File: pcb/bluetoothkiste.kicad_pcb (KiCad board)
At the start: 2 copper layers, 44.9 x 95.6 mm, 58 parts, among them J1 DB9_Female, J2 Screw_Terminal_01x03, J3 Conn_01x04_Female, J4 RJ45, J6 Conn_01x04_Female, U1 L7805, U2 MAX232

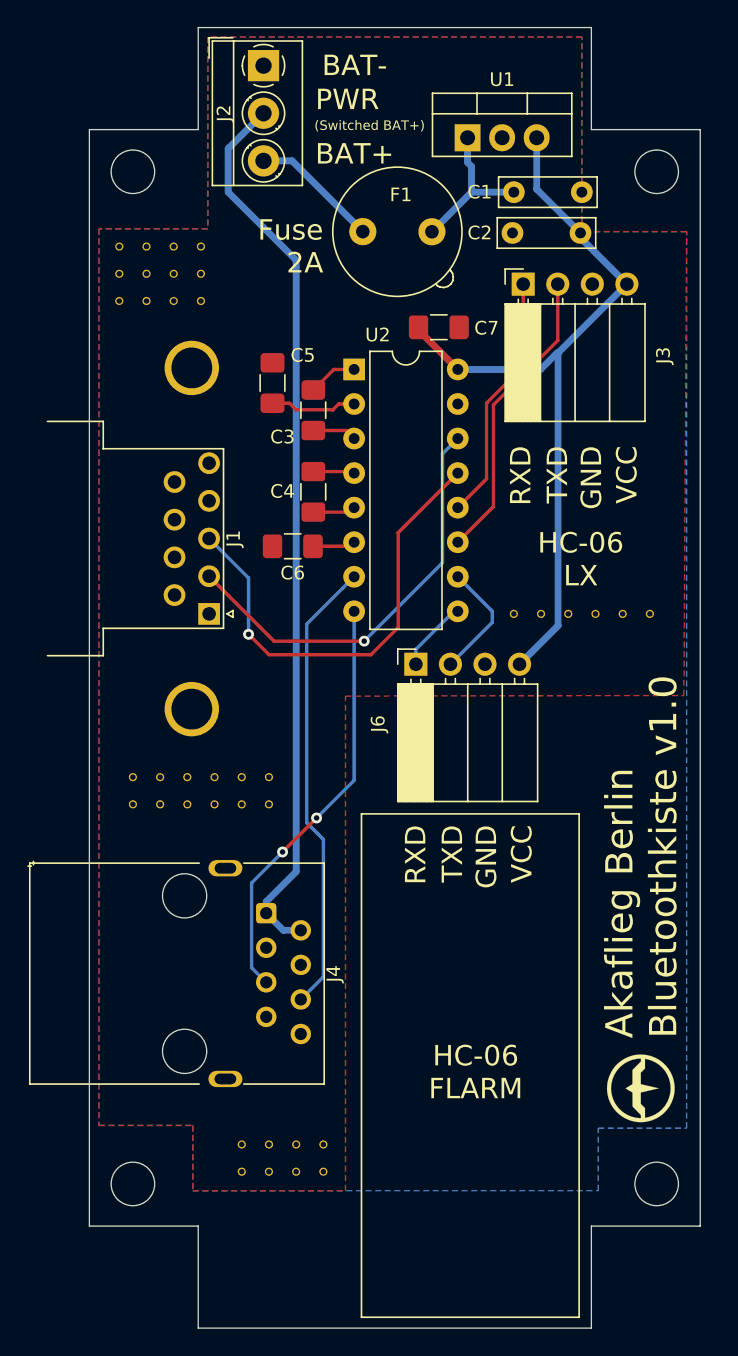
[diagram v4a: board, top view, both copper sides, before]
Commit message: layout updated
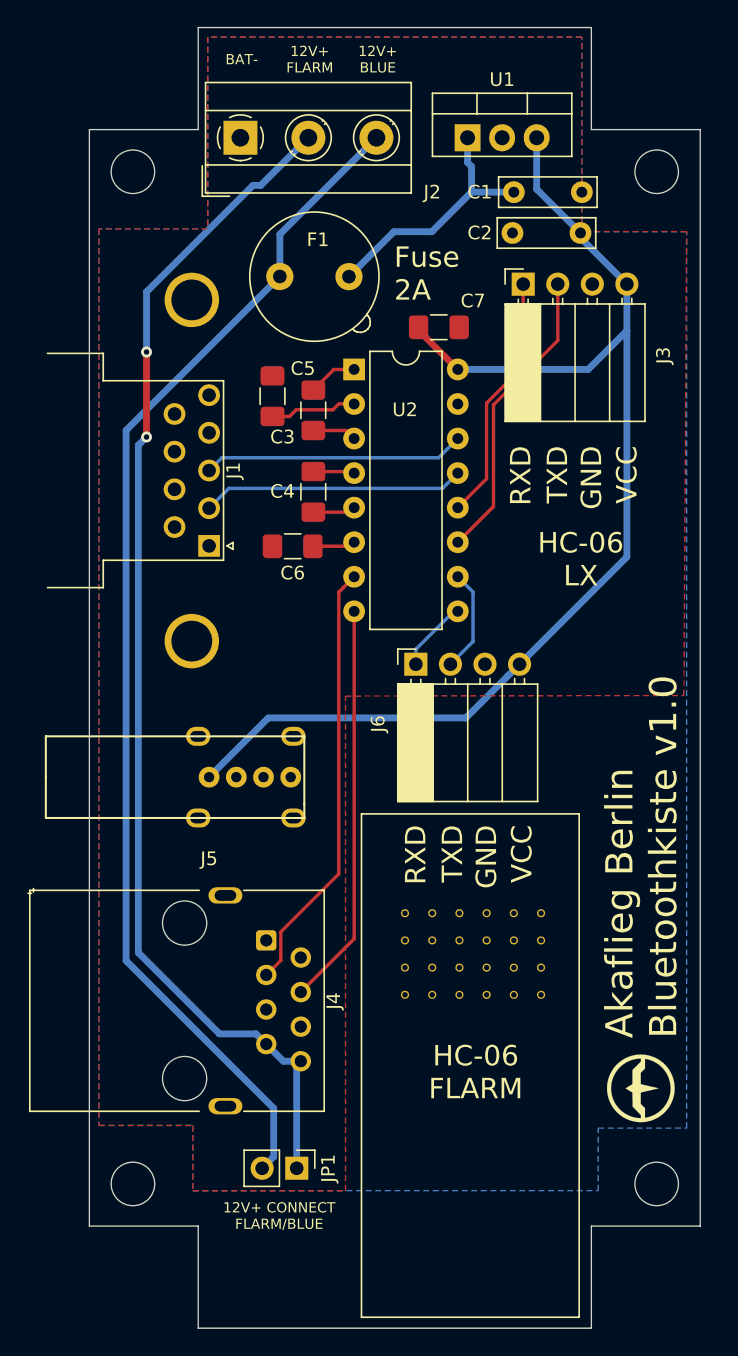
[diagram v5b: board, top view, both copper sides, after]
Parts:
- removed the REF** at (187.0, 60.0)
- removed the REF** at (169.0, 74.0)
- removed the REF** at (164.0, 33.0)
- removed the REF** at (158.0, 37.0)
- removed the REF** at (158.0, 35.0)
- removed the REF** at (164.0, 35.0)
- removed the REF** at (162.0, 37.0)
- removed the REF** at (160.0, 35.0)
- removed the REF** at (160.0, 37.0)
- removed the REF** at (162.0, 35.0)
- removed the REF** at (164.0, 37.0)
- removed the REF** at (191.0, 60.0)
- removed the REF** at (161.0, 74.0)
- removed the REF** at (161.0, 72.0)
- removed the REF** at (163.0, 72.0)
- removed the REF** at (165.0, 72.0)
- removed the REF** at (165.0, 74.0)
- removed the REF** at (163.0, 74.0)
- removed the REF** at (159.0, 72.0)
- removed the REF** at (159.0, 74.0)
- removed the REF** at (167.0, 101.0)
- removed the REF** at (195.0, 60.0)
- removed the REF** at (169.0, 101.0)
- removed the REF** at (171.0, 101.0)
- removed the REF** at (173.0, 101.0)
- removed the REF** at (173.0, 99.0)
- removed the REF** at (171.0, 99.0)
- removed the REF** at (169.0, 99.0)
- removed the REF** at (167.0, 99.0)
- removed the REF** at (162.0, 33.0)
- removed the REF** at (160.0, 33.0)
- removed the REF** at (158.0, 33.0)
- removed the REF** at (197.0, 60.0)
- removed the REF** at (189.0, 60.0)
- removed the REF** at (193.0, 60.0)
- removed the REF** at (169.0, 72.0)
- removed the REF** at (167.0, 74.0)
- removed the REF** at (167.0, 72.0)
- added J5: USB_A, JS_Local:USB_A_UPRIGHT_SEGOR, F.Cu at (164.6, 72.0)
- added JP1: Jumper, Connector_PinHeader_2.54mm:PinHeader_1x02_P2.54mm_Vertical, F.Cu at (171.0, 100.8)
- added REF**: VIA-0.6mm, JS_Local:VIA-0.6mm, F.Cu at (187.0, 82.0)
- added REF**: VIA-0.6mm, JS_Local:VIA-0.6mm, F.Cu at (179.0, 84.0)
- added REF**: VIA-0.6mm, JS_Local:VIA-0.6mm, F.Cu at (181.0, 84.0)
- added REF**: VIA-0.6mm, JS_Local:VIA-0.6mm, F.Cu at (183.0, 82.0)
- added REF**: VIA-0.6mm, JS_Local:VIA-0.6mm, F.Cu at (187.0, 88.0)
- added REF**: VIA-0.6mm, JS_Local:VIA-0.6mm, F.Cu at (189.0, 86.0)
- added REF**: VIA-0.6mm, JS_Local:VIA-0.6mm, F.Cu at (185.0, 86.0)
- added REF**: VIA-0.6mm, JS_Local:VIA-0.6mm, F.Cu at (187.0, 86.0)
- added REF**: VIA-0.6mm, JS_Local:VIA-0.6mm, F.Cu at (185.0, 88.0)
- added REF**: VIA-0.6mm, JS_Local:VIA-0.6mm, F.Cu at (189.0, 88.0)
- added REF**: VIA-0.6mm, JS_Local:VIA-0.6mm, F.Cu at (183.0, 88.0)
- added REF**: VIA-0.6mm, JS_Local:VIA-0.6mm, F.Cu at (185.0, 82.0)
- added REF**: VIA-0.6mm, JS_Local:VIA-0.6mm, F.Cu at (179.0, 88.0)
- added REF**: VIA-0.6mm, JS_Local:VIA-0.6mm, F.Cu at (181.0, 88.0)
- added REF**: VIA-0.6mm, JS_Local:VIA-0.6mm, F.Cu at (183.0, 86.0)
- added REF**: VIA-0.6mm, JS_Local:VIA-0.6mm, F.Cu at (181.0, 86.0)
- added REF**: VIA-0.6mm, JS_Local:VIA-0.6mm, F.Cu at (179.0, 86.0)
- added REF**: VIA-0.6mm, JS_Local:VIA-0.6mm, F.Cu at (189.0, 84.0)
- added REF**: VIA-0.6mm, JS_Local:VIA-0.6mm, F.Cu at (185.0, 84.0)
- added REF**: VIA-0.6mm, JS_Local:VIA-0.6mm, F.Cu at (187.0, 84.0)
- added REF**: VIA-0.6mm, JS_Local:VIA-0.6mm, F.Cu at (189.0, 82.0)
- added REF**: VIA-0.6mm, JS_Local:VIA-0.6mm, F.Cu at (179.0, 82.0)
- added REF**: VIA-0.6mm, JS_Local:VIA-0.6mm, F.Cu at (181.0, 82.0)
- added REF**: VIA-0.6mm, JS_Local:VIA-0.6mm, F.Cu at (183.0, 84.0)
- J2: footprint TerminalBlock_MetzConnect:TerminalBlock_MetzConnect_Type059_RT06303HBWC_1x03_P3.50mm_Horizontal -> TerminalBlock_MetzConnect:TerminalBlock_MetzConnect_Type055_RT01503HDWU_1x03_P5.00mm_Horizontal
- moved F1 6.94 mm to (169.8, 35.2)
- moved J2 5.57 mm to (166.9, 25.0), turned to 0 degrees
- moved J1 5.00 mm to (164.6, 55.0)
- moved J4 2.00 mm to (168.8, 84.0)
- moved C5 0.97 mm to (169.3, 44.0)
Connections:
- J1 pad 2: /LX-RX -> /LX-TX
- J1 pad 3: /LX-TX -> /LX-RX
- J4 pad 1: +12V -> GND
- J4 pad 2: +12V -> GND
- J4 pad 3: (no net) -> /FLARM-RX
- J4 pad 4: GND -> /FLARM-TX
- J4 pad 5: /FLARM-TX -> GND
- J4 pad 6: /FLARM-RX -> (no net)
- J4 pad 7: GND -> +12V
- J4 pad 8: GND -> +12V
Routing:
- net +12P: track 9.45 -> 88.2 mm
- net +5V: track 56.9 -> 88.9 mm
- net +12V: track 65.9 -> 88.7 mm, vias 0 -> 2
- net /LX-TX: track 33.9 -> 19.3 mm, vias 1 -> 0
- net /LX-RX: track 31.1 -> 19.3 mm, vias 1 -> 0
- net Net-(C1-Pad1): track 11.3 -> 18.8 mm
- net /FLARM-RX: track 33.7 -> 31.9 mm
- net /FLARM-TX: track 30.8 -> 29.6 mm, vias 2 -> 0
- net /FLARM-BT-TX: track 8.75 -> 7.59 mm
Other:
- net class Broader added: clearance 0.4, trace_width 0.5, via_dia 0.8, via_drill 0.4
- board text added: "12V+ BLUE"
- board text added: "12V+ CONNECT FLARM/BLUE"
- board text added: "12V+ FLARM"
- board text removed: "(Switched BAT+)"
- board text removed: "BAT+"
- board text removed: "PWR"

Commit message: dioden verpolungsschutz
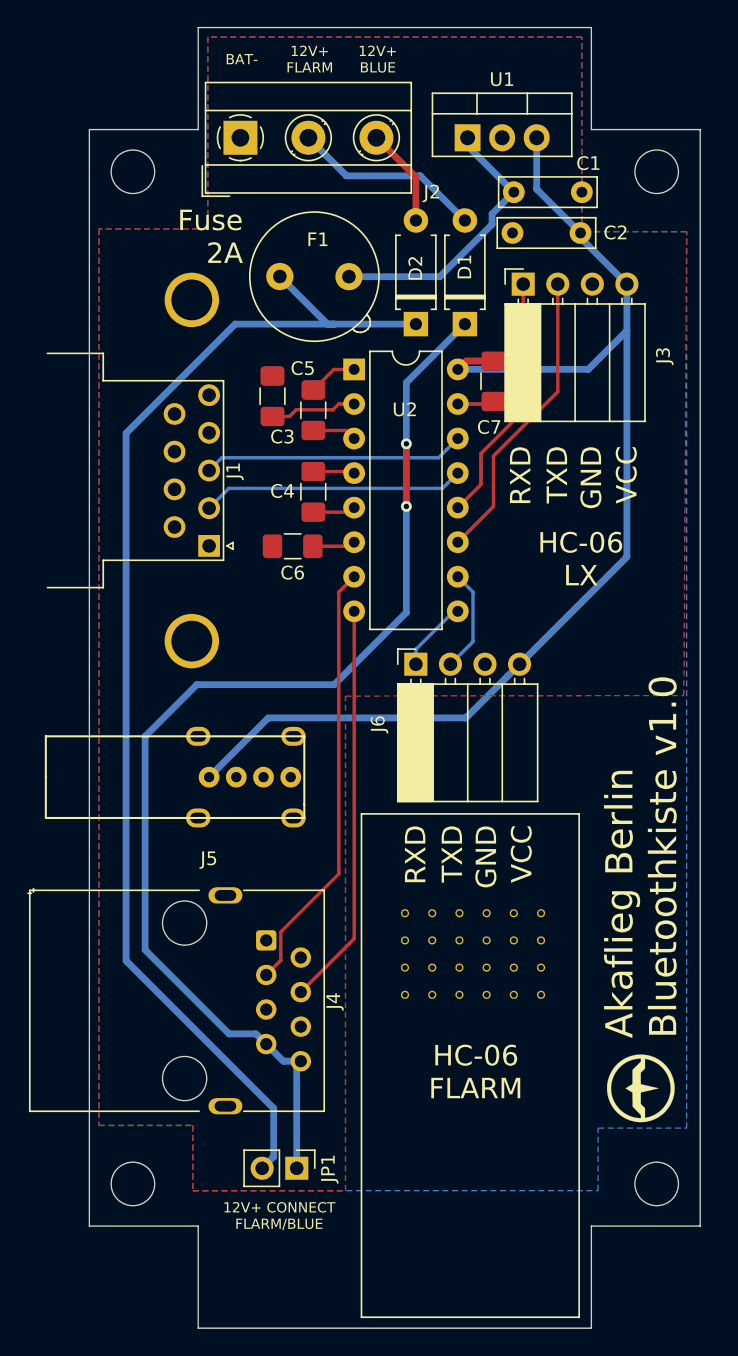
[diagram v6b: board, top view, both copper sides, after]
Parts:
- added D1: D, Diode_THT:D_A-405_P7.62mm_Horizontal, F.Cu at (183.4, 38.7)
- added D2: D, Diode_THT:D_A-405_P7.62mm_Horizontal, F.Cu at (179.8, 38.7)
- moved C7 5.64 mm to (185.5, 42.9), turned to 270 degrees
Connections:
- J2 pad 2: +12V -> Net-(D1-Pad2)
- J2 pad 3: +12P -> Net-(D2-Pad2)
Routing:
- net Net-(D1-Pad2): track 0.00 -> 14.0 mm
- net Net-(D2-Pad2): track 0.00 -> 7.28 mm
- net +12V: track 88.7 -> 84.5 mm
- net GND: track 0.00 -> 2.70 mm
- net Net-(C1-Pad1): track 18.8 -> 20.6 mm
- net +5V: track 88.9 -> 87.5 mm
- net +12P: track 88.2 -> 88.9 mm

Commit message: antennendistanz
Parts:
- removed the REF** at (187.0, 82.0)
- removed the REF** at (183.0, 82.0)
- removed the REF** at (187.0, 88.0)
- removed the REF** at (189.0, 86.0)
- removed the REF** at (185.0, 88.0)
- removed the REF** at (189.0, 88.0)
- removed the REF** at (183.0, 88.0)
- removed the REF** at (185.0, 82.0)
- removed the REF** at (189.0, 84.0)
- removed the REF** at (185.0, 84.0)
- removed the REF** at (187.0, 84.0)
- removed the REF** at (189.0, 82.0)
- removed the REF** at (183.0, 84.0)
- added REF**: VIA-0.6mm, JS_Local:VIA-0.6mm, F.Cu at (157.5, 37.0)
- added REF**: VIA-0.6mm, JS_Local:VIA-0.6mm, F.Cu at (172.0, 79.0)
- added REF**: VIA-0.6mm, JS_Local:VIA-0.6mm, F.Cu at (170.0, 77.0)
- added REF**: VIA-0.6mm, JS_Local:VIA-0.6mm, F.Cu at (168.0, 77.0)
- added REF**: VIA-0.6mm, JS_Local:VIA-0.6mm, F.Cu at (172.0, 59.0)
- added REF**: VIA-0.6mm, JS_Local:VIA-0.6mm, F.Cu at (170.0, 59.0)
- added REF**: VIA-0.6mm, JS_Local:VIA-0.6mm, F.Cu at (170.0, 61.0)
- added REF**: VIA-0.6mm, JS_Local:VIA-0.6mm, F.Cu at (172.0, 61.0)
- added REF**: VIA-0.6mm, JS_Local:VIA-0.6mm, F.Cu at (168.0, 61.0)
- added REF**: VIA-0.6mm, JS_Local:VIA-0.6mm, F.Cu at (157.5, 35.0)
- added REF**: VIA-0.6mm, JS_Local:VIA-0.6mm, F.Cu at (168.0, 59.0)
- added REF**: VIA-0.6mm, JS_Local:VIA-0.6mm, F.Cu at (159.5, 37.0)
- added REF**: VIA-0.6mm, JS_Local:VIA-0.6mm, F.Cu at (157.5, 33.0)
- added REF**: VIA-0.6mm, JS_Local:VIA-0.6mm, F.Cu at (159.5, 35.0)
- added REF**: VIA-0.6mm, JS_Local:VIA-0.6mm, F.Cu at (159.5, 33.0)
- added REF**: VIA-0.6mm, JS_Local:VIA-0.6mm, F.Cu at (170.0, 79.0)
- added REF**: VIA-0.6mm, JS_Local:VIA-0.6mm, F.Cu at (168.0, 79.0)
- added REF**: VIA-0.6mm, JS_Local:VIA-0.6mm, F.Cu at (172.0, 77.0)
- J3, J6: footprint Connector_PinSocket_2.54mm:PinSocket_1x04_P2.54mm_Horizontal -> Connector_PinHeader_2.54mm:PinHeader_1x04_P2.54mm_Vertical
- moved J3 34.3 mm to (196.0, 69.0), turned to 270 degrees
- moved G*** 32.6 mm to (167.0, 109.0), turned to 0 degrees
- moved REF** 27.5 mm to (170.0, 63.0)
- moved REF** 27.5 mm to (172.0, 63.0)
- moved REF** 27.5 mm to (168.0, 63.0)
- moved REF** 21.6 mm to (176.5, 66.5)
- moved REF** 21.6 mm to (178.5, 66.5)
- moved REF** 21.6 mm to (178.5, 64.5)
- moved REF** 21.6 mm to (176.5, 64.5)
- moved J6 13.3 mm to (180.0, 77.0)
- moved REF** 11.8 mm to (176.5, 70.5)
- moved REF** 11.8 mm to (178.5, 70.5)
- moved REF** 11.8 mm to (176.5, 72.5)
- moved REF** 11.8 mm to (178.5, 72.5)
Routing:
- net /FLARM-BT-RX: track 5.34 -> 18.7 mm, vias 0 -> 2
- net /FLARM-BT-TX: track 7.59 -> 20.8 mm, vias 0 -> 2
- net +5V: track 87.5 -> 98.5 mm
- net /LX-BT-RX: track 18.4 -> 22.7 mm, vias 0 -> 1
- net /LX-BT-TX: track 22.0 -> 20.0 mm, vias 0 -> 1
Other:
- board text added: "Akaflieg Berlin Bluetoothkiste v1.1"
- board text removed: "Akaflieg Berlin Bluetoothkiste v1.0"

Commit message: jumpers
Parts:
- removed the REF** at (168.0, 61.0)
- removed the REF** at (168.0, 59.0)
- removed the REF** at (168.0, 63.0)
- added J7: Conn_01x03, Connector_PinSocket_2.54mm:PinSocket_1x03_P2.54mm_Vertical, F.Cu at (195.0, 91.0)
- added J8: Conn_01x03, Connector_PinSocket_2.54mm:PinSocket_1x03_P2.54mm_Vertical, F.Cu at (195.0, 81.5)
- added JP2: Jumper, Connector_PinSocket_2.54mm:PinSocket_1x02_P2.54mm_Vertical, F.Cu at (194.5, 76.0)
- added REF**: VIA-0.6mm, JS_Local:VIA-0.6mm, F.Cu at (184.0, 71.5)
- added REF**: VIA-0.6mm, JS_Local:VIA-0.6mm, F.Cu at (187.0, 71.5)
- added REF**: VIA-0.6mm, JS_Local:VIA-0.6mm, F.Cu at (185.5, 71.5)
- added REF**: VIA-0.6mm, JS_Local:VIA-0.6mm, F.Cu at (193.0, 72.0)
- added REF**: VIA-0.6mm, JS_Local:VIA-0.6mm, F.Cu at (191.5, 72.0)
- added REF**: VIA-0.6mm, JS_Local:VIA-0.6mm, F.Cu at (190.0, 72.0)
- added REF**: VIA-0.6mm, JS_Local:VIA-0.6mm, F.Cu at (187.0, 73.0)
- added REF**: VIA-0.6mm, JS_Local:VIA-0.6mm, F.Cu at (185.5, 73.0)
- added REF**: VIA-0.6mm, JS_Local:VIA-0.6mm, F.Cu at (184.0, 73.0)
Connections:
- net /FLARM-TX renamed FLARM-TX
- J1 pad 2: /LX-TX -> /PIN2
- J1 pad 3: /LX-RX -> /PIN3
- J4 pad 3: /FLARM-RX -> Net-(J4-Pad3)
- U2 pad 13: /LX-TX -> LX-TX
- U2 pad 14: /LX-RX -> LX-RX
- U2 pad 7: /FLARM-RX -> FLARM-RX
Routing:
- net /PIN3: track 0.00 -> 66.1 mm, vias 0 -> 3
- net /PIN2: track 0.00 -> 65.4 mm, vias 0 -> 2
- net LX-RX: track 0.00 -> 56.3 mm, vias 0 -> 1
- net LX-TX: track 0.00 -> 44.1 mm, vias 0 -> 1
- net FLARM-RX: track 0.00 -> 37.4 mm, vias 0 -> 2
- net Net-(J4-Pad3): track 0.00 -> 33.2 mm, vias 0 -> 2
- net /FLARM-RX: track 31.9 -> 0.00 mm
- net /LX-TX: track 19.3 -> 0.00 mm
- net /LX-RX: track 19.3 -> 0.00 mm
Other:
- board text added: "12V+ BLUETOOTH"
- board text added: "Akaflieg Berlin Bluetoothkiste v1.2"
- board text added: "Connect FLARM and Bluetooth supply"
- board text added: "LX reading on"
- board text added: "LX transmitting on"
- board text added: "P2"
- board text added: "P3"
- board text added: "Transmit to FLARM"
- board text removed: "12V+ BLUE"
- board text removed: "12V+ CONNECT FLARM/BLUE"
- board text removed: "Akaflieg Berlin Bluetoothkiste v1.1"
